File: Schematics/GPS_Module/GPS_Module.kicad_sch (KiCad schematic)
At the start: 70 parts, among them J1 SATA Conn. (Male), J2 SWD_01x04_Pin, J4 Stack Male Edge Connector, J4 USB_C_Female_USB2_Small, Q1 AO3400A, SW1 SW_STM_RESET, SW2 SW_STM_BOOT_MODE, U1 STM32F103CBT6, U12 AMS1117-3.3, U2 W25Q128JVS, U4 LM66100DCKR, U5 LM66100DCKR, U6 LM66100DCKR, U8 ACS70331EOLC, U9 ISO1042BQDWVR, Y1 X322516MMB4SI

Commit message: Updated Debug/PPS/Power LED resistors
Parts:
- R11: value 560R -> 680R; LCSC C23204 -> C23228
- R5: value 820R -> 1.2k; LCSC C23253 -> C22765
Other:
- note added: "Vf=2.1V, I=1.8mA, R=680"
- note added: "Vf=2.8V, I=0.4mA, R=1.2k"
- note removed: "Vf=2.3V, I=1.8mA, R=560"
- note removed: "Vf=2.9V, I=0.5mA, R=820"
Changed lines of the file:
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@@
     (effects (font (size 1.27 1.27) (thickness 0.254) bold) (justify left bottom))
   )
-  (text "Vf=2.9V, I=0.5mA, R=820" (at 35.56 66.675 0)
-    (effects (font (size 1.27 1.27) italic) (justify left bottom))
-  )
   (text "STM32" (at 186.69 78.105 0)
     (effects (font (size 1.27 1.27) (thickness 0.254) bold) (justify left bottom))
@@
     (effects (font (size 1.27 1.27)) (justify left bottom))
   )
-  (text "Vf=2.3V, I=1.8mA, R=560" (at 378.46 113.03 0)
+  (text "Vf=2.1V, I=1.8mA, R=680" (at 378.46 113.03 0)
     (effects (font (size 1.27 1.27) italic) (justify left bottom))
   )
@@
     (effects (font (size 1.27 1.27)) (justify left bottom))
   )
-  (text "Vf=2.3V, I=1.8mA, R=560" (at 50.165 165.1 0)
-    (effects (font (size 1.27 1.27) italic) (justify left bottom))
-  )
   (text "Stack Edge Connector" (at 290.83 61.595 0)
     (effects (font (size 1.27 1.27) (thickness 0.254) bold) (justify left bottom))
@@
     (effects (font (size 1.27 1.27) (thickness 0.254) bold) (justify left bottom))
   )
+  (text "Vf=2.8V, I=0.4mA, R=1.2k" (at 35.56 66.675 0)
+    (effects (font (size 1.27 1.27) italic) (justify left bottom))
+  )
   (text "Place near edge of board (easier soldering)" (at 39.37 134.62 0)
     (effects (font (size 1.27 1.27) italic) (justify left bottom))
@@
     )
   )
-  (symbol (lib_id "Device:LED") (at 396.875 107.315 180) (unit 1)
-    (in_bom yes) (on_board yes) (dnp no)
-    (property "Reference" "D5" (at 396.875 100.965 0)
-      (effects (font (size 1.27 1.27)))
-    )
-    (property "Value" "DB_LED (YLW)" (at 396.875 103.505 0)
-      (effects (font (size 1.27 1.27)))
-    )
-    (property "Footprint" "LED_SMD:LED_0603_1608Metric" (at 396.875 107.315 0)
-      (effects (font (size 1.27 1.27)) hide)
-    )
-    (property "Datasheet" "~" (at 396.875 107.315 0)
-      (effects (font (size 1.27 1.27)) hide)
-    )
-    (property "LCSC" "C72038" (at 396.875 107.315 0)
-      (effects (font (size 1.27 1.27)) hide)
-    )
-    (pin "1")
-    (pin "2")
-    (instances
-      (project "Communications_Module"
-        (path "/ace06731-9b48-45c3-868d-c65fed1a8f9b"
-          (reference "D5") (unit 1)
-        )
-      )
-      (project "GPS_Module"
-        (path "/c9a01778-8bed-4fe7-bd5a-975b80c0ed6a"
-          (reference "D8") (unit 1)
-        )
-      )
-    )
-  )
   (symbol (lib_id "Device:R") (at 348.615 127.635 270) (unit 1)
     (in_bom yes) (on_board yes) (dnp no) (fields_autoplaced)
@@
     )
   )
-  (symbol (lib_id "Device:LED") (at 52.07 62.23 180) (unit 1)
-    (in_bom yes) (on_board yes) (dnp no)
-    (property "Reference" "D1" (at 52.07 55.88 0)
-      (effects (font (size 1.27 1.27)))
-    )
-    (property "Value" "PWR_LED (GRN)" (at 52.07 58.42 0)
-      (effects (font (size 1.27 1.27)))
-    )
-    (property "Footprint" "LED_SMD:LED_0805_2012Metric" (at 52.07 62.23 0)
-      (effects (font (size 1.27 1.27)) hide)
-    )
-    (property "Datasheet" "~" (at 52.07 62.23 0)
-      (effects (font (size 1.27 1.27)) hide)
-    )
-    (property "LCSC" "C2297" (at 52.07 62.23 0)
-      (effects (font (size 1.27 1.27)) hide)
-    )
-    (pin "1")
-    (pin "2")
-    (instances
-      (project "Communications_Module"
-        (path "/ace06731-9b48-45c3-868d-c65fed1a8f9b"
-          (reference "D1") (unit 1)
-        )
-      )
-      (project "GPS_Module"
-        (path "/c9a01778-8bed-4fe7-bd5a-975b80c0ed6a"
-          (reference "D4") (unit 1)
-        )
-      )
-    )
-  )
   (symbol (lib_id "Device:C") (at 393.7 149.225 0) (unit 1)
     (in_bom yes) (on_board yes) (dnp no) (fields_autoplaced)
@@
     )
   )
-  (symbol (lib_id "Device:R") (at 385.445 107.315 270) (unit 1)
-    (in_bom yes) (on_board yes) (dnp no) (fields_autoplaced)
-    (property "Reference" "R11" (at 385.445 102.1547 90)
-      (effects (font (size 1.27 1.27)))
-    )
-    (property "Value" "560R" (at 385.445 104.5789 90)
-      (effects (font (size 1.27 1.27)))
-    )
-    (property "Footprint" "Resistor_SMD:R_0603_1608Metric" (at 385.445 105.537 90)
-      (effects (font (size 1.27 1.27)) hide)
-    )
-    (property "Datasheet" "~" (at 385.445 107.315 0)
-      (effects (font (size 1.27 1.27)) hide)
-    )
-    (property "LCSC" "C23204" (at 385.445 107.315 0)
-      (effects (font (size 1.27 1.27)) hide)
-    )
-    (pin "1")
-    (pin "2")
-    (instances
-      (project "Communications_Module"
-        (path "/ace06731-9b48-45c3-868d-c65fed1a8f9b"
-          (reference "R11") (unit 1)
-        )
-      )
-      (project "GPS_Module"
-        (path "/c9a01778-8bed-4fe7-bd5a-975b80c0ed6a"
-          (reference "R7") (unit 1)
-        )
-      )
-    )
-  )
   (symbol (lib_id "Device:R") (at 376.555 41.275 270) (unit 1)
     (in_bom yes) (on_board yes) (dnp no) (fields_autoplaced)
@@
     )
   )
+  (symbol (lib_id "Device:LED") (at 396.875 107.315 180) (unit 1)
+    (in_bom yes) (on_board yes) (dnp no)
+    (property "Reference" "D5" (at 396.875 100.965 0)
+      (effects (font (size 1.27 1.27)))
+    )
+    (property "Value" "DB_LED (YLW)" (at 396.875 103.505 0)
+      (effects (font (size 1.27 1.27)))
+    )
+    (property "Footprint" "LED_SMD:LED_0603_1608Metric" (at 396.875 107.315 0)
+      (effects (font (size 1.27 1.27)) hide)
+    )
+    (property "Datasheet" "~" (at 396.875 107.315 0)
+      (effects (font (size 1.27 1.27)) hide)
+    )
+    (property "LCSC" "C72038" (at 396.875 107.315 0)
+      (effects (font (size 1.27 1.27)) hide)
+    )
+    (pin "1")
+    (pin "2")
+    (instances
+      (project "Communications_Module"
+        (path "/ace06731-9b48-45c3-868d-c65fed1a8f9b"
+          (reference "D5") (unit 1)
+        )
+      )
+      (project "GPS_Module"
+        (path "/c9a01778-8bed-4fe7-bd5a-975b80c0ed6a"
+          (reference "D8") (unit 1)
+        )
+      )
+    )
+  )
   (symbol (lib_id "Memory_Flash:W25Q128JVS") (at 179.07 44.45 0) (unit 1)
     (in_bom yes) (on_board yes) (dnp no) (fields_autoplaced)
@@
     )
   )
-  (symbol (lib_id "Device:R") (at 40.64 62.23 270) (unit 1)
-    (in_bom yes) (on_board yes) (dnp no) (fields_autoplaced)
-    (property "Reference" "R5" (at 40.64 57.0697 90)
+  (symbol (lib_id "Device:R") (at 385.445 107.315 270) (unit 1)
+    (in_bom yes) (on_board yes) (dnp no)
+    (property "Reference" "R11" (at 385.445 104.775 90)
       (effects (font (size 1.27 1.27)))
     )
-    (property "Value" "820R" (at 40.64 59.4939 90)
+    (property "Value" "680R" (at 385.445 107.315 90)
       (effects (font (size 1.27 1.27)))
     )
-    (property "Footprint" "Resistor_SMD:R_0603_1608Metric" (at 40.64 60.452 90)
+    (property "Footprint" "Resistor_SMD:R_0603_1608Metric" (at 385.445 105.537 90)
       (effects (font (size 1.27 1.27)) hide)
     )
-    (property "Datasheet" "~" (at 40.64 62.23 0)
+    (property "Datasheet" "~" (at 385.445 107.315 0)
       (effects (font (size 1.27 1.27)) hide)
     )
-    (property "LCSC" "C23253" (at 40.64 62.23 0)
+    (property "LCSC" "C23228" (at 385.445 107.315 0)
       (effects (font (size 1.27 1.27)) hide)
     )
@@
       (project "Communications_Module"
         (path "/ace06731-9b48-45c3-868d-c65fed1a8f9b"
-          (reference "R5") (unit 1)
+          (reference "R11") (unit 1)
         )
       )
       (project "GPS_Module"
         (path "/c9a01778-8bed-4fe7-bd5a-975b80c0ed6a"
-          (reference "R4") (unit 1)
+          (reference "R7") (unit 1)
         )
       )
@@
     )
   )
+  (symbol (lib_id "Device:LED") (at 52.07 62.23 180) (unit 1)
+    (in_bom yes) (on_board yes) (dnp no)
+    (property "Reference" "D1" (at 52.07 55.88 0)
+      (effects (font (size 1.27 1.27)))
+    )
+    (property "Value" "PWR_LED (GRN)" (at 52.07 58.42 0)
+      (effects (font (size 1.27 1.27)))
+    )
+    (property "Footprint" "LED_SMD:LED_0805_2012Metric" (at 52.07 62.23 0)
+      (effects (font (size 1.27 1.27)) hide)
+    )
+    (property "Datasheet" "~" (at 52.07 62.23 0)
+      (effects (font (size 1.27 1.27)) hide)
+    )
+    (property "LCSC" "C2297" (at 52.07 62.23 0)
+      (effects (font (size 1.27 1.27)) hide)
+    )
+    (pin "1")
+    (pin "2")
+    (instances
+      (project "Communications_Module"
+        (path "/ace06731-9b48-45c3-868d-c65fed1a8f9b"
+          (reference "D1") (unit 1)
+        )
+      )
+      (project "GPS_Module"
+        (path "/c9a01778-8bed-4fe7-bd5a-975b80c0ed6a"
+          (reference "D4") (unit 1)
+        )
+      )
+    )
+  )
   (symbol (lib_id "ISO1042BQDWVQ1:ISO1042BQDWVQ1") (at 378.46 210.82 0) (unit 1)
     (in_bom yes) (on_board yes) (dnp no) (fields_autoplaced)
@@
         )
       )
+    )
+  )
+  (symbol (lib_id "Device:R") (at 40.64 62.23 270) (unit 1)
+    (in_bom yes) (on_board yes) (dnp no)
+    (property "Reference" "R5" (at 40.64 59.69 90)
+      (effects (font (size 1.27 1.27)))
+    )
+    (property "Value" "1.2k" (at 40.64 62.23 90)
+      (effects (font (size 1.27 1.27)))
+    )
+    (property "Footprint" "Resistor_SMD:R_0603_1608Metric" (at 40.64 60.452 90)
+      (effects (font (size 1.27 1.27)) hide)
+    )
+    (property "Datasheet" "~" (at 40.64 62.23 0)
+      (effects (font (size 1.27 1.27)) hide)
+    )
+    (property "LCSC" "C22765" (at 40.64 62.23 0)
+      (effects (font (size 1.27 1.27)) hide)
+    )
+    (pin "1")
+    (pin "2")
+    (instances
+      (project "Communications_Module"
+        (path "/ace06731-9b48-45c3-868d-c65fed1a8f9b"
+          (reference "R5") (unit 1)
+        )
+      )
+      (project "GPS_Module"
+        (path "/c9a01778-8bed-4fe7-bd5a-975b80c0ed6a"
+          (reference "R4") (unit 1)
+        )
+      )

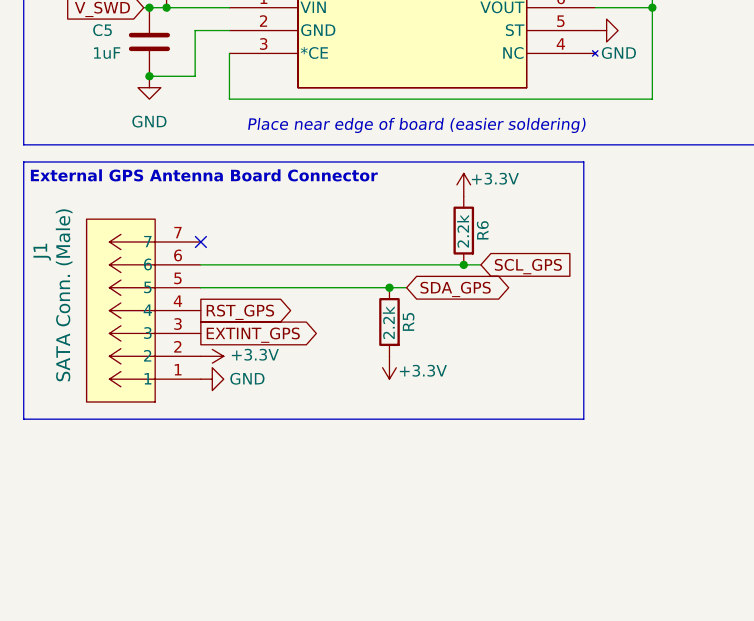
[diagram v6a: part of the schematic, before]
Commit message: Replaced SATA connector on GPS Module+Antenna
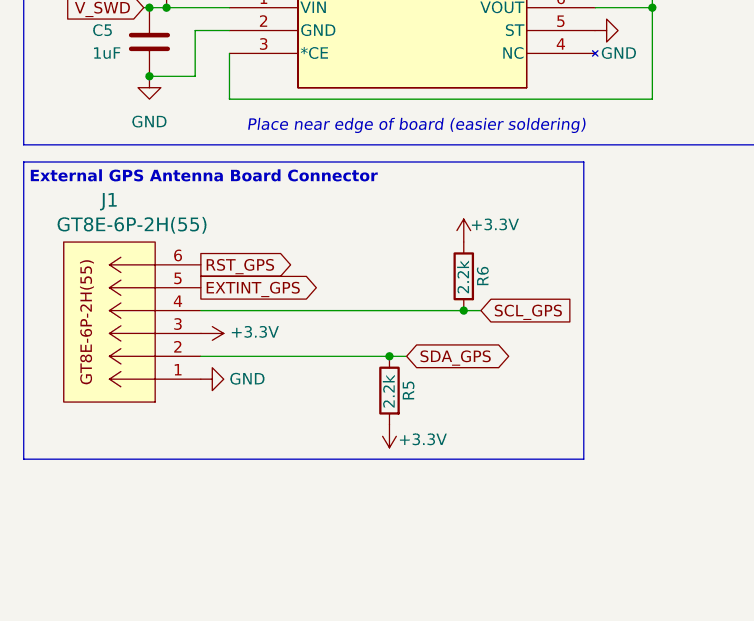
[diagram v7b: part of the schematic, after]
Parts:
- removed J1: SATA Conn. (Male), footprints:CONN_47080-4001_MOL_SATA, symbol CONN_47080-4001_MOL_SATA:470804001
- added J1: GT8E-6P-2H(55), footprints:CONN_GT8E-6P-2H(55), symbol CONN_GT8E-6P-2H(55):GT8E-6P-2H(55)
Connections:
- net +3.3V: now also J1.3
- net EXTINT_GPS: now also J1.5
- net GND: now also J1.1
- net RST_GPS: now also J1.6
- net SCL_GPS: now also J1.4
- net SDA_GPS: now also J1.2
- no-connect marks 21 -> 20
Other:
- moved on the sheet: R5, R6

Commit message: Bump revision number to V2.0 & V1.2
GPS module is V2.0, Antenna PCB is V1.2
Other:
- title: QRET 23-24 SRAD GPS Module -> QRET 23-25 SRAD GPS Module
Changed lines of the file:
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@@
   (paper "B")
   (title_block
-    (title "QRET 23-24 SRAD GPS Module")
-    (date "2025-02-15")
-    (rev "V1.0")
+    (title "QRET 23-25 SRAD GPS Module")
+    (date "2025-02-16")
+    (rev "V2.0")
     (company "Queen's Rocket Engineering Team")
     (comment 1 "Contributors: Tristan Alderson, Kennan Bays")
